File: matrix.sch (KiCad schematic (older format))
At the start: 8 parts

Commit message: update matrix
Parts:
- removed D? (x4): D_Small, Diode_SMD:D_SOD-123, symbol Device:D_Small
- removed MX? (x4): MX-NoLED, MX_Alps_Hybrid:MX-1U, symbol MX_Alps_Hybrid:MX-NoLED
- added D1, D10, D11, D12, D13, D14, D15, D16, D17, D18, D19, D2, D20, D21, D22, D23, D24, D25, D26, D27, D28, D29, D3, D30, D31, D32, D33, D34, D35, D36, D37, D38, D39, D4, D40, D41, D42, D43, D44, D45, D46, D47, D48, D49, D5, D50, D51, D52, D53, D54, D55, D56, D57, D58, D59, D6, D60, D61, D7, D8, D9: D_Small, Diode_SMD:D_SOD-123, symbol Device:D_Small
- added MX1: ESC, MX_Alps_Hybrid:MX-1U, symbol MX_Alps_Hybrid:MX-NoLED
- added MX10: #9, MX_Alps_Hybrid:MX-1U, symbol MX_Alps_Hybrid:MX-NoLED
- added MX11: #0, MX_Alps_Hybrid:MX-1U, symbol MX_Alps_Hybrid:MX-NoLED
- added MX12: -_, MX_Alps_Hybrid:MX-1U, symbol MX_Alps_Hybrid:MX-NoLED
- added MX13: =+, MX_Alps_Hybrid:MX-1U, symbol MX_Alps_Hybrid:MX-NoLED
- added MX14: BSPC, MX_Alps_Hybrid:MX-1U, symbol MX_Alps_Hybrid:MX-NoLED
- added MX15: TAB, MX_Alps_Hybrid:MX-1U, symbol MX_Alps_Hybrid:MX-NoLED
- added MX16: Q, MX_Alps_Hybrid:MX-1U, symbol MX_Alps_Hybrid:MX-NoLED
- added MX17: W, MX_Alps_Hybrid:MX-1U, symbol MX_Alps_Hybrid:MX-NoLED
- added MX18: E, MX_Alps_Hybrid:MX-1U, symbol MX_Alps_Hybrid:MX-NoLED
- added MX19: R, MX_Alps_Hybrid:MX-1U, symbol MX_Alps_Hybrid:MX-NoLED
- added MX2: #1, MX_Alps_Hybrid:MX-1U, symbol MX_Alps_Hybrid:MX-NoLED
- added MX20: T, MX_Alps_Hybrid:MX-1U, symbol MX_Alps_Hybrid:MX-NoLED
- added MX21: Y, MX_Alps_Hybrid:MX-1U, symbol MX_Alps_Hybrid:MX-NoLED
- added MX22: U, MX_Alps_Hybrid:MX-1U, symbol MX_Alps_Hybrid:MX-NoLED
- added MX23: I, MX_Alps_Hybrid:MX-1U, symbol MX_Alps_Hybrid:MX-NoLED
- added MX24: O, MX_Alps_Hybrid:MX-1U, symbol MX_Alps_Hybrid:MX-NoLED
- added MX25: P, MX_Alps_Hybrid:MX-1U, symbol MX_Alps_Hybrid:MX-NoLED
- added MX26: [{, MX_Alps_Hybrid:MX-1U, symbol MX_Alps_Hybrid:MX-NoLED
- added MX27: ]}, MX_Alps_Hybrid:MX-1U, symbol MX_Alps_Hybrid:MX-NoLED
- added MX28: \\|, MX_Alps_Hybrid:MX-1U, symbol MX_Alps_Hybrid:MX-NoLED
- added MX29: CAPS, MX_Alps_Hybrid:MX-1U, symbol MX_Alps_Hybrid:MX-NoLED
- added MX3: #2, MX_Alps_Hybrid:MX-1U, symbol MX_Alps_Hybrid:MX-NoLED
- added MX30: A, MX_Alps_Hybrid:MX-1U, symbol MX_Alps_Hybrid:MX-NoLED
- added MX31: S, MX_Alps_Hybrid:MX-1U, symbol MX_Alps_Hybrid:MX-NoLED
- added MX32: D, MX_Alps_Hybrid:MX-1U, symbol MX_Alps_Hybrid:MX-NoLED
- added MX33: F, MX_Alps_Hybrid:MX-1U, symbol MX_Alps_Hybrid:MX-NoLED
- added MX34: G, MX_Alps_Hybrid:MX-1U, symbol MX_Alps_Hybrid:MX-NoLED
- added MX35: H, MX_Alps_Hybrid:MX-1U, symbol MX_Alps_Hybrid:MX-NoLED
- added MX36: J, MX_Alps_Hybrid:MX-1U, symbol MX_Alps_Hybrid:MX-NoLED
- added MX37: K, MX_Alps_Hybrid:MX-1U, symbol MX_Alps_Hybrid:MX-NoLED
- added MX38: L, MX_Alps_Hybrid:MX-1U, symbol MX_Alps_Hybrid:MX-NoLED
- added MX39: ;:, MX_Alps_Hybrid:MX-1U, symbol MX_Alps_Hybrid:MX-NoLED
- added MX4: #3, MX_Alps_Hybrid:MX-1U, symbol MX_Alps_Hybrid:MX-NoLED
- added MX40: '\", MX_Alps_Hybrid:MX-1U, symbol MX_Alps_Hybrid:MX-NoLED
- added MX41: ENTER, MX_Alps_Hybrid:MX-1U, symbol MX_Alps_Hybrid:MX-NoLED
- added MX42: LSHIFT, MX_Alps_Hybrid:MX-1U, symbol MX_Alps_Hybrid:MX-NoLED
- added MX43: Z, MX_Alps_Hybrid:MX-1U, symbol MX_Alps_Hybrid:MX-NoLED
- added MX44: X, MX_Alps_Hybrid:MX-1U, symbol MX_Alps_Hybrid:MX-NoLED
- added MX45: C, MX_Alps_Hybrid:MX-1U, symbol MX_Alps_Hybrid:MX-NoLED
- added MX46: V, MX_Alps_Hybrid:MX-1U, symbol MX_Alps_Hybrid:MX-NoLED
- added MX47: B, MX_Alps_Hybrid:MX-1U, symbol MX_Alps_Hybrid:MX-NoLED
- added MX48: N, MX_Alps_Hybrid:MX-1U, symbol MX_Alps_Hybrid:MX-NoLED
- added MX49: M, MX_Alps_Hybrid:MX-1U, symbol MX_Alps_Hybrid:MX-NoLED
- added MX5: #4, MX_Alps_Hybrid:MX-1U, symbol MX_Alps_Hybrid:MX-NoLED
- added MX50: ,<, MX_Alps_Hybrid:MX-1U, symbol MX_Alps_Hybrid:MX-NoLED
- added MX51: .>, MX_Alps_Hybrid:MX-1U, symbol MX_Alps_Hybrid:MX-NoLED
- added MX52: /?, MX_Alps_Hybrid:MX-1U, symbol MX_Alps_Hybrid:MX-NoLED
- added MX53: RSHIFT, MX_Alps_Hybrid:MX-1U, symbol MX_Alps_Hybrid:MX-NoLED
- added MX54: LCTRL, MX_Alps_Hybrid:MX-1U, symbol MX_Alps_Hybrid:MX-NoLED
- added MX55, MX59: CMD, MX_Alps_Hybrid:MX-1U, symbol MX_Alps_Hybrid:MX-NoLED
- added MX56: LALT, MX_Alps_Hybrid:MX-1U, symbol MX_Alps_Hybrid:MX-NoLED
- added MX57: SPACE, MX_Alps_Hybrid:MX-1U, symbol MX_Alps_Hybrid:MX-NoLED
- added MX58: RALT, MX_Alps_Hybrid:MX-1U, symbol MX_Alps_Hybrid:MX-NoLED
- added MX6: #5, MX_Alps_Hybrid:MX-1U, symbol MX_Alps_Hybrid:MX-NoLED
- added MX60: FN, MX_Alps_Hybrid:MX-1U, symbol MX_Alps_Hybrid:MX-NoLED
- added MX61: RCTRL, MX_Alps_Hybrid:MX-1U, symbol MX_Alps_Hybrid:MX-NoLED
- added MX7: #6, MX_Alps_Hybrid:MX-1U, symbol MX_Alps_Hybrid:MX-NoLED
- added MX8: #7, MX_Alps_Hybrid:MX-1U, symbol MX_Alps_Hybrid:MX-NoLED
- added MX9: #8, MX_Alps_Hybrid:MX-1U, symbol MX_Alps_Hybrid:MX-NoLED
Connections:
- net COL0: now also MX1.1 (COL), MX15.1 (COL), MX29.1 (COL), MX42.1 (COL), MX54.1 (COL)
- net COL1: now also MX16.1 (COL), MX2.1 (COL), MX30.1 (COL), MX43.1 (COL), MX55.1 (COL)
- net ROW0: now also D1.1 (K), D10.1 (K), D11.1 (K), D12.1 (K), D13.1 (K), D14.1 (K), D2.1 (K), D3.1 (K), D4.1 (K), D5.1 (K), D6.1 (K), D7.1 (K), D8.1 (K), D9.1 (K)
- net ROW1: now also D15.1 (K), D16.1 (K), D17.1 (K), D18.1 (K), D19.1 (K), D20.1 (K), D21.1 (K), D22.1 (K), D23.1 (K), D24.1 (K), D25.1 (K), D26.1 (K), D27.1 (K), D28.1 (K)
- new net: D1.2 (A), MX1.2 (ROW)
- new net: D2.2 (A), MX2.2 (ROW)
- new net: D3.2 (A), MX3.2 (ROW)
- new net: D15.2 (A), MX15.2 (ROW)
- new net: D16.2 (A), MX16.2 (ROW)
- new net: D17.2 (A), MX17.2 (ROW)
- new net: D29.2 (A), MX29.2 (ROW)
- new net: D30.2 (A), MX30.2 (ROW)
- new net: D31.2 (A), MX31.2 (ROW)
- new net: D4.2 (A), MX4.2 (ROW)
- new net: D5.2 (A), MX5.2 (ROW)
- new net: D6.2 (A), MX6.2 (ROW)
- new net: D18.2 (A), MX18.2 (ROW)
- new net: D19.2 (A), MX19.2 (ROW)
- new net: D20.2 (A), MX20.2 (ROW)
- new net: D32.2 (A), MX32.2 (ROW)
- new net: D33.2 (A), MX33.2 (ROW)
- new net: D34.2 (A), MX34.2 (ROW)
- new net: D7.2 (A), MX7.2 (ROW)
- new net: D8.2 (A), MX8.2 (ROW)
- new net: D9.2 (A), MX9.2 (ROW)
- new net: D21.2 (A), MX21.2 (ROW)
- new net: D22.2 (A), MX22.2 (ROW)
- new net: D23.2 (A), MX23.2 (ROW)
- new net: D35.2 (A), MX35.2 (ROW)
- new net: D36.2 (A), MX36.2 (ROW)
- new net: D37.2 (A), MX37.2 (ROW)
- new net: D10.2 (A), MX10.2 (ROW)
- new net: D11.2 (A), MX11.2 (ROW)
- new net: D12.2 (A), MX12.2 (ROW)
- new net: D24.2 (A), MX24.2 (ROW)
- new net: D25.2 (A), MX25.2 (ROW)
- new net: D26.2 (A), MX26.2 (ROW)
- new net: D38.2 (A), MX38.2 (ROW)
- new net: D39.2 (A), MX39.2 (ROW)
- new net: D40.2 (A), MX40.2 (ROW)
- new net: D13.2 (A), MX13.2 (ROW)
- new net: D14.2 (A), MX14.2 (ROW)
- new net: D27.2 (A), MX27.2 (ROW)
- new net: D28.2 (A), MX28.2 (ROW)
- new net: D41.2 (A), MX41.2 (ROW)
- new net: D42.2 (A), MX42.2 (ROW)
- new net: D43.2 (A), MX43.2 (ROW)
- new net: D44.2 (A), MX44.2 (ROW)
- new net: D54.2 (A), MX54.2 (ROW)
- new net: D55.2 (A), MX55.2 (ROW)
- new net: D56.2 (A), MX56.2 (ROW)
- new net: D45.2 (A), MX45.2 (ROW)
- new net: D46.2 (A), MX46.2 (ROW)
- new net: D47.2 (A), MX47.2 (ROW)
- new net: D48.2 (A), MX48.2 (ROW)
- new net: D49.2 (A), MX49.2 (ROW)
- new net: D50.2 (A), MX50.2 (ROW)
- new net: D57.2 (A), MX57.2 (ROW)
- new net: D51.2 (A), MX51.2 (ROW)
- new net: D52.2 (A), MX52.2 (ROW)
- new net: D58.2 (A), MX58.2 (ROW)
- new net: D59.2 (A), MX59.2 (ROW)
- new net: D53.2 (A), MX53.2 (ROW)
- new net: D60.2 (A), MX60.2 (ROW)
- new net: D61.2 (A), MX61.2 (ROW)
- new net COL10: MX11.1 (COL), MX25.1 (COL), MX39.1 (COL), MX52.1 (COL), MX58.1 (COL)
- new net COL11: MX12.1 (COL), MX26.1 (COL), MX40.1 (COL), MX59.1 (COL)
- new net COL12: MX13.1 (COL), MX27.1 (COL), MX60.1 (COL)
- new net COL13: MX14.1 (COL), MX28.1 (COL), MX41.1 (COL), MX53.1 (COL), MX61.1 (COL)
- new net COL2: MX17.1 (COL), MX3.1 (COL), MX31.1 (COL), MX44.1 (COL), MX56.1 (COL)
- new net COL3: MX18.1 (COL), MX32.1 (COL), MX4.1 (COL), MX45.1 (COL)
- new net COL4: MX19.1 (COL), MX33.1 (COL), MX46.1 (COL), MX5.1 (COL)
- new net COL5: MX20.1 (COL), MX34.1 (COL), MX47.1 (COL), MX6.1 (COL)
- new net COL6: MX21.1 (COL), MX35.1 (COL), MX48.1 (COL), MX57.1 (COL), MX7.1 (COL)
- new net COL7: MX22.1 (COL), MX36.1 (COL), MX49.1 (COL), MX8.1 (COL)
- new net COL8: MX23.1 (COL), MX37.1 (COL), MX50.1 (COL), MX9.1 (COL)
- new net COL9: MX10.1 (COL), MX24.1 (COL), MX38.1 (COL), MX51.1 (COL)
- new net ROW2: D29.1 (K), D30.1 (K), D31.1 (K), D32.1 (K), D33.1 (K), D34.1 (K), D35.1 (K), D36.1 (K), D37.1 (K), D38.1 (K), D39.1 (K), D40.1 (K), D41.1 (K)
- new net ROW3: D42.1 (K), D43.1 (K), D44.1 (K), D45.1 (K), D46.1 (K), D47.1 (K), D48.1 (K), D49.1 (K), D50.1 (K), D51.1 (K), D52.1 (K), D53.1 (K)
- new net ROW4: D54.1 (K), D55.1 (K), D56.1 (K), D57.1 (K), D58.1 (K), D59.1 (K), D60.1 (K), D61.1 (K)

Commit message: update pcb
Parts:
- MX1, MX10, MX11, MX12, MX13, MX16, MX17, MX18, MX19, MX2, MX20, MX21, MX22, MX23, MX24, MX25, MX26, MX27, MX3, MX30, MX31, MX32, MX33, MX34, MX35, MX36, MX37, MX38, MX39, MX4, MX40, MX43, MX44, MX45, MX46, MX47, MX48, MX49, MX5, MX50, MX51, MX52, MX6, MX7, MX8, MX9: footprint MX_Alps_Hybrid:MX-1U -> MX_Alps_Hybrid:MX-1U-NoLED
- MX14: footprint MX_Alps_Hybrid:MX-1U -> MX_Alps_Hybrid:MX-2U-NoLED
- MX15, MX28: footprint MX_Alps_Hybrid:MX-1U -> MX_Alps_Hybrid:MX-1.5U-NoLED
- MX29: footprint MX_Alps_Hybrid:MX-1U -> MX_Alps_Hybrid:MX-1.75U-NoLED
- MX41, MX42: footprint MX_Alps_Hybrid:MX-1U -> MX_Alps_Hybrid:MX-2.25U-NoLED
- MX53: footprint MX_Alps_Hybrid:MX-1U -> MX_Alps_Hybrid:MX-2.75U-NoLED
- MX54, MX56, MX58, MX60, MX61: footprint MX_Alps_Hybrid:MX-1U -> MX_Alps_Hybrid:MX-1.25U-NoLED
- MX55: value CMD -> LCMD; footprint MX_Alps_Hybrid:MX-1U -> MX_Alps_Hybrid:MX-1.25U-NoLED
- MX57: footprint MX_Alps_Hybrid:MX-1U -> MX_Alps_Hybrid:MX-6.25U-NoLED
- MX59: value CMD -> RCMD; footprint MX_Alps_Hybrid:MX-1U -> MX_Alps_Hybrid:MX-1.25U-NoLED

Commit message: update pcb
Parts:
- MX57: footprint MX_Alps_Hybrid:MX-6.25U-NoLED -> MX_Alps_Hybrid:MX-6.25U-ReversedStabilizers-NoLED
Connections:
- net COL10: now also MX59.1 (COL); no longer MX58.1 (COL)
- net COL11: now also MX60.1 (COL); no longer MX59.1 (COL)
- net COL12: no longer MX60.1 (COL)
- net COL5: now also MX57.1 (COL)
- net COL6: no longer MX57.1 (COL)
- net COL9: now also MX58.1 (COL)
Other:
- moved on the sheet: D57, D58, D59, D60, MX57, MX58, MX59, MX60
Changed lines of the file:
@@
 L MX_Alps_Hybrid:MX-NoLED MX?
 U 1 1 6060D600
-P 5850 4650
+P 5350 4650
 AR Path="/6060D600" Ref="MX?"  Part="1"
 AR Path="/604A8D0E/6060D600" Ref="MX57"  Part="1"
 AR Path="/6050FBE2/6060D600" Ref="MX?"  Part="1"
-F 0 "MX57" H 5650 4700 60  0000 C CNN
-F 1 "SPACE" H 5650 4650 20  0000 C CNN
-F 2 "MX_Alps_Hybrid:MX-6.25U-NoLED" H 5225 4625 60  0001 C CNN
-F 3 "" H 5225 4625 60  0001 C CNN
-	1    5850 4650
+F 0 "MX57" H 5150 4700 60  0000 C CNN
+F 1 "SPACE" H 5150 4650 20  0000 C CNN
+F 2 "MX_Alps_Hybrid:MX-6.25U-ReversedStabilizers-NoLED" H 4725 4625 60  0001 C CNN
+F 3 "" H 4725 4625 60  0001 C CNN
+	1    5350 4650
 	1    0    0    -1
 $EndComp
@@
 L Device:D_Small D?
 U 1 1 6060D60A
-P 5600 4900
+P 5100 4900
 AR Path="/6060D60A" Ref="D?"  Part="1"
 AR Path="/604A8D0E/6060D60A" Ref="D57"  Part="1"
 AR Path="/6050FBE2/6060D60A" Ref="D?"  Part="1"
-F 0 "D57" V 5646 4830 50  0000 R CNN
-F 1 "D_Small" V 5555 4830 50  0000 R CNN
-F 2 "Diode_SMD:D_SOD-123" V 5600 4900 50  0001 C CNN
-F 3 "~" V 5600 4900 50  0001 C CNN
-	1    5600 4900
-	0    -1   -1   0
-$EndComp
-Wire Wire Line
-	5600 4800 5800 4800
+F 0 "D57" V 5146 4830 50  0000 R CNN
+F 1 "D_Small" V 5055 4830 50  0000 R CNN
+F 2 "Diode_SMD:D_SOD-123" V 5100 4900 50  0001 C CNN
+F 3 "~" V 5100 4900 50  0001 C CNN
+	1    5100 4900
+	0    -1   -1   0
+$EndComp
+Wire Wire Line
+	5100 4800 5300 4800
 $Comp
 L MX_Alps_Hybrid:MX-NoLED MX?
@@
 L MX_Alps_Hybrid:MX-NoLED MX?
 U 1 1 6060D693
-P 7850 4650
+P 7350 4650
 AR Path="/6060D693" Ref="MX?"  Part="1"
 AR Path="/604A8D0E/6060D693" Ref="MX58"  Part="1"
 AR Path="/6050FBE2/6060D693" Ref="MX?"  Part="1"
-F 0 "MX58" H 7650 4700 60  0000 C CNN
-F 1 "RALT" H 7650 4650 20  0000 C CNN
+F 0 "MX58" H 7150 4700 60  0000 C CNN
+F 1 "RALT" H 7150 4650 20  0000 C CNN
+F 2 "MX_Alps_Hybrid:MX-1.25U-NoLED" H 6725 4625 60  0001 C CNN
+F 3 "" H 6725 4625 60  0001 C CNN
+	1    7350 4650
+	1    0    0    -1
+$EndComp
+$Comp
+L Device:D_Small D?
+U 1 1 6060D69D
+P 7100 4900
+AR Path="/6060D69D" Ref="D?"  Part="1"
+AR Path="/604A8D0E/6060D69D" Ref="D58"  Part="1"
+AR Path="/6050FBE2/6060D69D" Ref="D?"  Part="1"
+F 0 "D58" V 7146 4830 50  0000 R CNN
+F 1 "D_Small" V 7055 4830 50  0000 R CNN
+F 2 "Diode_SMD:D_SOD-123" V 7100 4900 50  0001 C CNN
+F 3 "~" V 7100 4900 50  0001 C CNN
+	1    7100 4900
+	0    -1   -1   0
+$EndComp
+Wire Wire Line
+	7100 4800 7300 4800
+$Comp
+L MX_Alps_Hybrid:MX-NoLED MX?
+U 1 1 6060D6A8
+P 7850 4650
+AR Path="/6060D6A8" Ref="MX?"  Part="1"
+AR Path="/604A8D0E/6060D6A8" Ref="MX59"  Part="1"
+AR Path="/6050FBE2/6060D6A8" Ref="MX?"  Part="1"
+F 0 "MX59" H 7650 4700 60  0000 C CNN
+F 1 "RCMD" H 7650 4650 20  0000 C CNN
 F 2 "MX_Alps_Hybrid:MX-1.25U-NoLED" H 7225 4625 60  0001 C CNN
 F 3 "" H 7225 4625 60  0001 C CNN
@@
 $Comp
 L Device:D_Small D?
-U 1 1 6060D69D
+U 1 1 6060D6B2
 P 7600 4900
-AR Path="/6060D69D" Ref="D?"  Part="1"
-AR Path="/604A8D0E/6060D69D" Ref="D58"  Part="1"
-AR Path="/6050FBE2/6060D69D" Ref="D?"  Part="1"
-F 0 "D58" V 7646 4830 50  0000 R CNN
+AR Path="/6060D6B2" Ref="D?"  Part="1"
+AR Path="/604A8D0E/6060D6B2" Ref="D59"  Part="1"
+AR Path="/6050FBE2/6060D6B2" Ref="D?"  Part="1"
+F 0 "D59" V 7646 4830 50  0000 R CNN
 F 1 "D_Small" V 7555 4830 50  0000 R CNN
 F 2 "Diode_SMD:D_SOD-123" V 7600 4900 50  0001 C CNN
@@
 Wire Wire Line
 	7600 4800 7800 4800
-$Comp
-L MX_Alps_Hybrid:MX-NoLED MX?
-U 1 1 6060D6A8
-P 8350 4650
-AR Path="/6060D6A8" Ref="MX?"  Part="1"
-AR Path="/604A8D0E/6060D6A8" Ref="MX59"  Part="1"
-AR Path="/6050FBE2/6060D6A8" Ref="MX?"  Part="1"
-F 0 "MX59" H 8150 4700 60  0000 C CNN
-F 1 "RCMD" H 8150 4650 20  0000 C CNN
-F 2 "MX_Alps_Hybrid:MX-1.25U-NoLED" H 7725 4625 60  0001 C CNN
-F 3 "" H 7725 4625 60  0001 C CNN
-	1    8350 4650
-	1    0    0    -1
-$EndComp
-$Comp
-L Device:D_Small D?
-U 1 1 6060D6B2
-P 8100 4900
-AR Path="/6060D6B2" Ref="D?"  Part="1"
-AR Path="/604A8D0E/6060D6B2" Ref="D59"  Part="1"
-AR Path="/6050FBE2/6060D6B2" Ref="D?"  Part="1"
-F 0 "D59" V 8146 4830 50  0000 R CNN
-F 1 "D_Small" V 8055 4830 50  0000 R CNN
-F 2 "Diode_SMD:D_SOD-123" V 8100 4900 50  0001 C CNN
-F 3 "~" V 8100 4900 50  0001 C CNN
-	1    8100 4900
-	0    -1   -1   0
-$EndComp
-Wire Wire Line
-	8100 4800 8300 4800
 $Comp
 L MX_Alps_Hybrid:MX-NoLED MX?
@@
 L MX_Alps_Hybrid:MX-NoLED MX?
 U 1 1 6060D6FC
-P 8850 4650
+P 8350 4650
 AR Path="/6060D6FC" Ref="MX?"  Part="1"
 AR Path="/604A8D0E/6060D6FC" Ref="MX60"  Part="1"
 AR Path="/6050FBE2/6060D6FC" Ref="MX?"  Part="1"
-F 0 "MX60" H 8650 4700 60  0000 C CNN
-F 1 "FN" H 8650 4650 20  0000 C CNN
-F 2 "MX_Alps_Hybrid:MX-1.25U-NoLED" H 8225 4625 60  0001 C CNN
-F 3 "" H 8225 4625 60  0001 C CNN
-	1    8850 4650
+F 0 "MX60" H 8150 4700 60  0000 C CNN
+F 1 "FN" H 8150 4650 20  0000 C CNN
+F 2 "MX_Alps_Hybrid:MX-1.25U-NoLED" H 7725 4625 60  0001 C CNN
+F 3 "" H 7725 4625 60  0001 C CNN
+	1    8350 4650
 	1    0    0    -1
 $EndComp
@@
 L Device:D_Small D?
 U 1 1 6060D706
-P 8600 4900
+P 8100 4900
 AR Path="/6060D706" Ref="D?"  Part="1"
 AR Path="/604A8D0E/6060D706" Ref="D60"  Part="1"
 AR Path="/6050FBE2/6060D706" Ref="D?"  Part="1"
-F 0 "D60" V 8646 4830 50  0000 R CNN
-F 1 "D_Small" V 8555 4830 50  0000 R CNN
-F 2 "Diode_SMD:D_SOD-123" V 8600 4900 50  0001 C CNN
-F 3 "~" V 8600 4900 50  0001 C CNN
-	1    8600 4900
-	0    -1   -1   0
-$EndComp
-Wire Wire Line
-	8600 4800 8800 4800
+F 0 "D60" V 8146 4830 50  0000 R CNN
+F 1 "D_Small" V 8055 4830 50  0000 R CNN
+F 2 "Diode_SMD:D_SOD-123" V 8100 4900 50  0001 C CNN
+F 3 "~" V 8100 4900 50  0001 C CNN
+	1    8100 4900
+	0    -1   -1   0
+$EndComp
+Wire Wire Line
+	8100 4800 8300 4800
 $Comp
 L MX_Alps_Hybrid:MX-NoLED MX?
@@
 Wire Wire Line
 	9500 4100 9500 4600
-Wire Wire Line
-	9000 4600 9000 3100
 Connection ~ 9000 2600
 Wire Wire Line
 	9000 2600 9000 2000
-Connection ~ 9000 3100
 Wire Wire Line
 	9000 3100 9000 2600
@@
 Wire Wire Line
 	8500 3100 8500 3600
-Connection ~ 8500 3600
-Wire Wire Line
-	8500 3600 8500 4600
 Wire Wire Line
 	8000 2000 8000 2600
@@
 Wire Wire Line
 	8000 3600 8000 4100
-Connection ~ 8000 4100
-Wire Wire Line
-	8000 4100 8000 4600
 Wire Wire Line
 	7500 2000 7500 2600
@@
 Wire Wire Line
 	6000 3600 6000 4100
-Connection ~ 6000 4100
-Wire Wire Line
-	6000 4100 6000 4600
 Wire Wire Line
 	5500 2000 5500 2600
@@
 Connection ~ 3600 5000
 Wire Wire Line
-	3600 5000 5600 5000
-Connection ~ 5600 5000
-Wire Wire Line
-	5600 5000 7600 5000
+	3600 5000 5100 5000
 Connection ~ 7600 5000
 Wire Wire Line
 	7600 5000 8100 5000
 Connection ~ 8100 5000
-Wire Wire Line
-	8100 5000 8600 5000
-Connection ~ 8600 5000
-Wire Wire Line
-	8600 5000 9100 5000
 Text HLabel 2000 3000 0    50   BiDi ~ 0
 ROW0
@@
 Text HLabel 9500 2000 1    50   BiDi ~ 0
 COL13
+Connection ~ 7100 5000
+Wire Wire Line
+	7100 5000 7600 5000
+Wire Wire Line
+	8100 5000 9100 5000
+Wire Wire Line
+	7500 4100 7500 4600
+Connection ~ 7500 4100
+Wire Wire Line
+	8000 4600 8000 4100
+Connection ~ 8000 4100
+Wire Wire Line
+	8500 4600 8500 3600
+Connection ~ 8500 3600
+Connection ~ 5100 5000
+Wire Wire Line
+	5100 5000 7100 5000
+Wire Wire Line
+	5500 4100 5500 4600
+Connection ~ 5500 4100
 $EndSCHEMATC

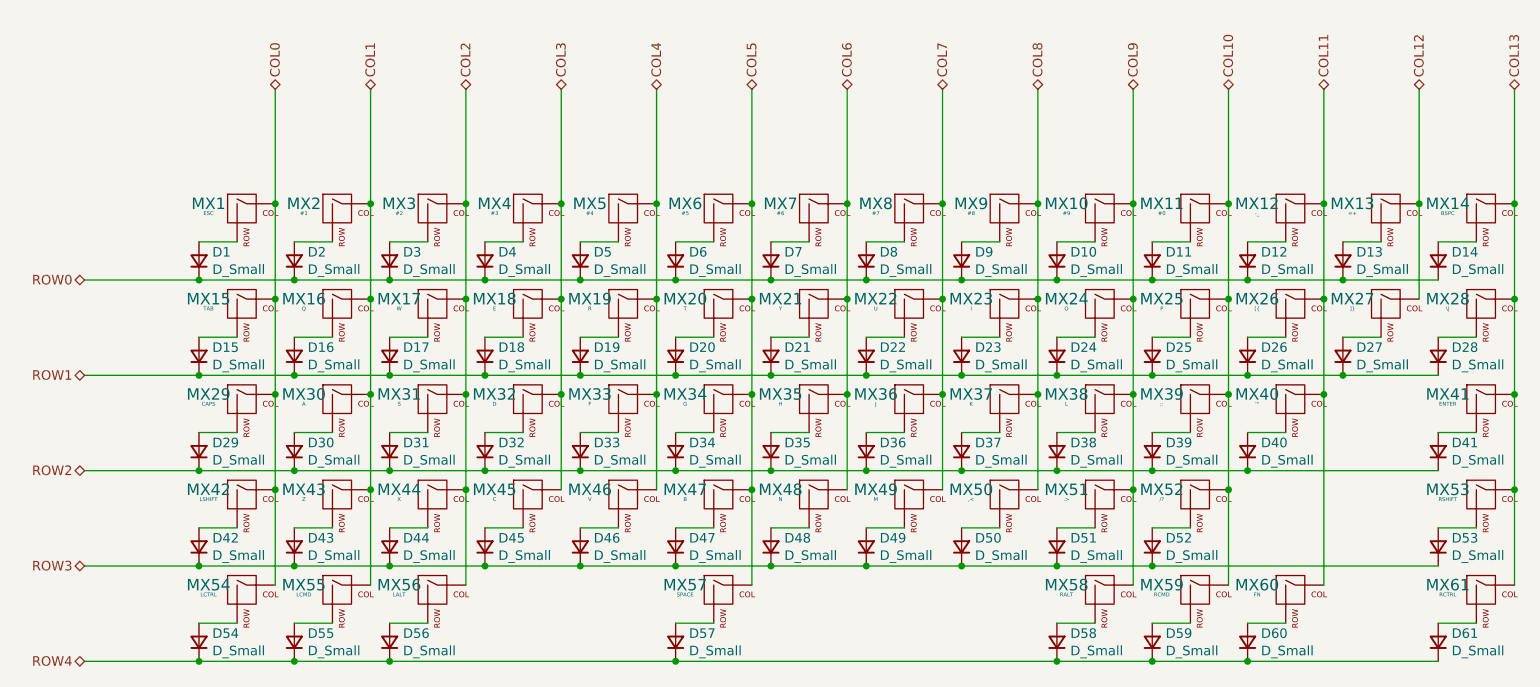
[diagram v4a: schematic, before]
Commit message: update diode
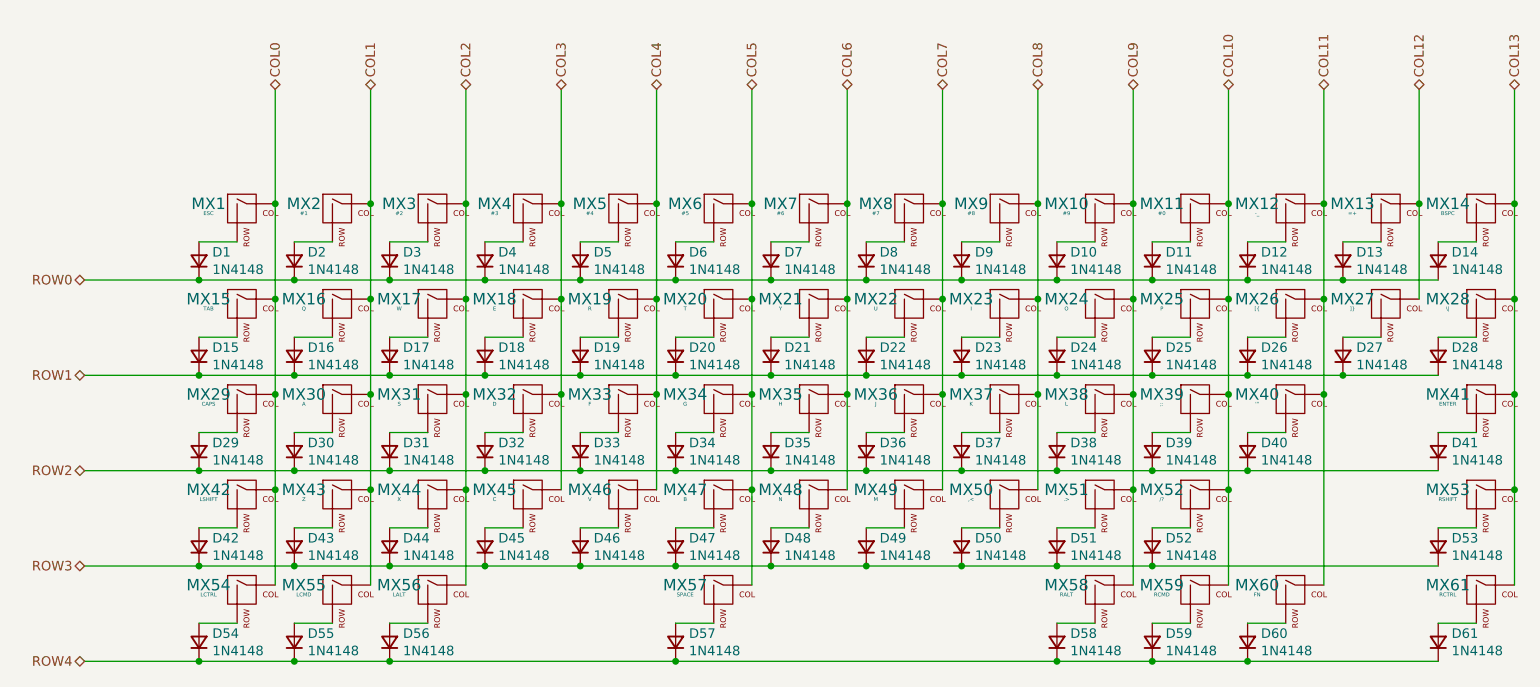
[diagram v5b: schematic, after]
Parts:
- D1, D10, D11, D12, D13, D14, D15, D16, D17, D18, D19, D2, D20, D21, D22, D23, D24, D25, D26, D27, D28, D29, D3, D30, D31, D32, D33, D34, D35, D36, D37, D38, D39, D4, D40, D41, D42, D43, D44, D45, D46, D47, D48, D49, D5, D50, D51, D52, D53, D54, D55, D56, D57, D58, D59, D6, D60, D61, D7, D8, D9: value D_Small -> 1N4148
